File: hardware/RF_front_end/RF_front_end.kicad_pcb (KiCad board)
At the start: 2 copper layers, 42 parts, among them J1 Conn_Coaxial, J2 Conn_Coaxial, Q1 SI1539CDL-T1-GE3, U1 F2972NEGK, U2 TRF37D73, U3 F2972NEGK, U4 RFSA3413, U5 TRF37D73

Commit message: More work on front end
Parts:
- removed C6: 100n, Capacitor_SMD:C_0402_1005Metric
- removed R4: 10k, Resistor_SMD:R_0402_1005Metric
- removed R5: 0, Resistor_SMD:R_0402_1005Metric
- added C21: 10u, Capacitor_SMD:C_0402_1005Metric, F.Cu at (103.8, 107.5)
- added C22: 100n, Capacitor_SMD:C_0402_1005Metric, F.Cu at (105.0, 107.5)
- added C23: 100n, Capacitor_SMD:C_0402_1005Metric, F.Cu at (108.5, 109.8)
- added C24: C, Capacitor_SMD:C_0402_1005Metric, F.Cu at (91.2, 121.5)
- added C25: C, Capacitor_SMD:C_0402_1005Metric, F.Cu at (91.2, 122.8)
- added C26: C, Capacitor_SMD:C_0402_1005Metric, F.Cu at (93.2, 125.0)
- added C27: C, Capacitor_SMD:C_0402_1005Metric, F.Cu at (91.2, 127.2)
- added C28: C, Capacitor_SMD:C_0402_1005Metric, F.Cu at (91.2, 128.5)
- added C29: C, Capacitor_SMD:C_0402_1005Metric, F.Cu at (94.0, 130.0)
- added C30: C, Capacitor_SMD:C_0402_1005Metric, F.Cu at (96.2, 128.0)
- added C31: C, Capacitor_SMD:C_0402_1005Metric, F.Cu at (97.5, 128.0)
- added C32: C, Capacitor_SMD:C_0402_1005Metric, F.Cu at (100.5, 127.5)
- added C33: C, Capacitor_SMD:C_0402_1005Metric, F.Cu at (99.5, 125.2)
- added C34: C, Capacitor_SMD:C_0402_1005Metric, F.Cu at (99.5, 124.0)
- added FB6: FerriteBead_Small, Inductor_SMD:L_0402_1005Metric, F.Cu at (101.2, 107.5)
- added L5: L, Inductor_SMD:L_0603_1608Metric, F.Cu at (91.8, 125.0)
- added L6: L, Inductor_SMD:L_0603_1608Metric, F.Cu at (94.0, 128.5)
- added L7: L, Inductor_SMD:L_0603_1608Metric, F.Cu at (99.0, 127.5)
- added U6: TRF37D73, Package_SON:WSON-8-1EP_2x2mm_P0.5mm_EP0.9x1.6mm, F.Cu at (103.8, 110.0)
- C13: value C -> 100n; footprint Capacitor_SMD:C_0603_1608Metric -> Capacitor_SMD:C_0402_1005Metric
- C14: value C -> 10u; footprint Capacitor_SMD:C_0603_1608Metric -> Capacitor_SMD:C_0402_1005Metric
- C18, C8: value 10u -> 100n; footprint Capacitor_SMD:C_0603_1608Metric -> Capacitor_SMD:C_0402_1005Metric
- C2, C3: footprint Capacitor_SMD:C_0603_1608Metric -> Capacitor_SMD:C_0402_1005Metric
- C9: value 100n -> 10u
- FB2, FB5: footprint Inductor_SMD:L_0603_1608Metric -> Inductor_SMD:L_0402_1005Metric
- L3: value L -> 0603LS-392X_R_
- R2: value 0 -> 10k
- U1, U3: value F2972NEGK -> TRF37D73; footprint RF_WUT:Renesas_QFN-12-1EP_2x2mm_P0.5mm_EP1.1x1.1mm -> Package_SON:WSON-8-1EP_2x2mm_P0.5mm_EP0.9x1.6mm
- U2: value TRF37D73 -> F2972NEGK; footprint Package_SON:WSON-8-1EP_2x2mm_P0.5mm_EP0.9x1.6mm -> RF_WUT:Renesas_QFN-12-1EP_2x2mm_P0.5mm_EP1.1x1.1mm
- U4: value RFSA3413 -> F2972NEGK; footprint Package_DFN_QFN:QFN-16-1EP_3x3mm_P0.5mm_EP1.7x1.7mm_ThermalVias -> RF_WUT:Renesas_QFN-12-1EP_2x2mm_P0.5mm_EP1.1x1.1mm
- U5: value TRF37D73 -> RFSA3413; footprint Package_SON:WSON-8-1EP_2x2mm_P0.5mm_EP0.9x1.6mm -> Package_DFN_QFN:QFN-16-1EP_3x3mm_P0.5mm_EP1.7x1.7mm_ThermalVias
- moved C9 96.9 mm to (89.0, 115.8), turned to 90 degrees
- moved FB5 95.0 mm to (95.2, 119.5)
- moved C4 94.8 mm to (101.8, 121.8)
- moved C11 92.6 mm to (91.8, 119.8), turned to -90 degrees
- moved C8 92.2 mm to (87.8, 115.8), turned to 90 degrees
- moved R1 83.3 mm to (105.8, 117.2), turned to 90 degrees
- moved U5 71.8 mm to (96.5, 115.5), turned to 90 degrees
- moved FB1 71.0 mm to (86.5, 115.8), turned to -90 degrees
- moved R3 66.4 mm to (96.8, 109.2), turned to 90 degrees
- moved C12 65.3 mm to (99.0, 119.8)
- moved C20 65.1 mm to (102.5, 107.5), turned to 90 degrees
- moved C14 64.7 mm to (101.2, 117.2), turned to 180 degrees
- moved C16 64.1 mm to (103.0, 112.8), turned to 180 degrees
- moved C18 63.9 mm to (95.2, 118.2), turned to 180 degrees
- moved C15 63.4 mm to (101.2, 116.0), turned to 180 degrees
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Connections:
- net Net-(C3-Pad1) renamed /20dB Gain Block/RFIN
- C10 pad 2: Net-(C10-Pad2) -> GND
- C11 pad 2: GND -> /20dB Gain Block/RFOUT
- C12 pad 2: Net-(C12-Pad2) -> GND
- C13 pad 1: Net-(C12-Pad2) -> Net-(C13-Pad1)
- C14 pad 1: Net-(C14-Pad1) -> Net-(C13-Pad1)
- C15 pad 1: Net-(C15-Pad1) -> Net-(C13-Pad1)
- C16 pad 2: Net-(C16-Pad2) -> /20dB Gain Block1/RFOUT
- C18 pad 1: Net-(C17-Pad1) -> Net-(C18-Pad1)
- C19 pad 1: Net-(C17-Pad1) -> Net-(C19-Pad1)
- C19 pad 2: GND -> /Adjustable Attenuator/RFOUT
- C20 pad 2: Net-(C20-Pad2) -> GND
- C4 pad 1: Net-(C4-Pad1) -> /RF Switch/RF1
- C4 pad 2: GND -> /20dB Gain Block1/RFIN
- C5 pad 1: Net-(C5-Pad1) -> /RF Switch/RF2
- C5 pad 2: Net-(C5-Pad2) -> /Adjustable Attenuator/RFIN
- C7 pad 1: Net-(C7-Pad1) -> /RF Switch1/RFC
- C7 pad 2: Net-(C7-Pad2) -> /20dB Gain Block2/RFIN
- C8 pad 1: Net-(C6-Pad1) -> Net-(C10-Pad1)
- C9 pad 1: Net-(C6-Pad1) -> Net-(C10-Pad1)
- FB1 pad 2: Net-(C4-Pad1) -> Net-(C10-Pad1)
- FB2 pad 2: Net-(C6-Pad1) -> Net-(C12-Pad1)
- FB3 pad 2: Net-(C11-Pad1) -> Net-(C13-Pad1)
- FB4 pad 2: Net-(C15-Pad1) -> Net-(C17-Pad1)
- FB5 pad 2: Net-(C17-Pad1) -> Net-(C18-Pad1)
- J2 pad 1: Net-(C20-Pad2) -> /20dB Gain Block2/RFOUT
- L2 pad 1: Net-(L2-Pad1) -> Net-(C10-Pad1)
- L2 pad 2: Net-(C10-Pad1) -> Net-(C11-Pad1)
- L3 pad 1: Net-(C12-Pad2) -> Net-(C13-Pad1)
- L3 pad 2: Net-(C14-Pad1) -> Net-(C16-Pad1)
- L4 pad 1: Net-(L4-Pad1) -> Net-(C20-Pad1)
- L4 pad 2: Net-(C20-Pad1) -> Net-(C23-Pad1)
- Q1 pad 2: Net-(Q1-Pad2) -> /ATT_EN
- Q1 pad 6: Net-(Q1-Pad6) -> /RF Switch1/VCTL
- R1 pad 1: Net-(Q1-Pad2) -> /ATT_EN
- R1 pad 2: Net-(R1-Pad2) -> /20dB Gain Block1/PWRDN
- R2 pad 1: Net-(C6-Pad1) -> /ATT_EN
- R2 pad 2: Net-(L2-Pad1) -> GND
- R3 pad 1: Net-(Q1-Pad2) -> +3V3
- R3 pad 2: GND -> /RF Switch1/VCTL
- U1 pad 1: GND -> Net-(C10-Pad1)
- U1 pad 5: Net-(C5-Pad1) -> /20dB Gain Block/PWRDN
- U1 pad 7: Net-(Q1-Pad2) -> Net-(C11-Pad1)
- U1 pad 8: Net-(C4-Pad1) -> GND
- U1 pad 9: Net-(C4-Pad1) -> GND
- U2 pad 1: Net-(C6-Pad1) -> GND
- U2 pad 2: Net-(C5-Pad2) -> /Generic Filter/RFOUT
- U2 pad 5: Net-(R1-Pad2) -> /RF Switch/RF1
- U2 pad 7: Net-(C10-Pad1) -> /ATT_EN
- U2 pad 8: GND -> Net-(C12-Pad1)
- U2 pad 9: GND -> Net-(C12-Pad1)
- U3 pad 1: GND -> Net-(C13-Pad1)
- U3 pad 2: Net-(C12-Pad1) -> /20dB Gain Block1/RFIN
- U3 pad 5: Net-(C7-Pad2) -> /20dB Gain Block1/PWRDN
- U3 pad 7: Net-(Q1-Pad6) -> Net-(C16-Pad1)
- U3 pad 8: Net-(C11-Pad1) -> GND
- U3 pad 9: Net-(C11-Pad1) -> GND
- U4 pad 1: Net-(C15-Pad1) -> GND
- U4 pad 11: Net-(C16-Pad1) -> /20dB Gain Block1/RFOUT
- U4 pad 13: unconnected-(U4-Pad13) -> GND
- U4 pad 2: Net-(C14-Pad1) -> /RF Switch1/RFC
- U4 pad 5: GND -> /Adjustable Attenuator/RFOUT
- U4 pad 7: GND -> /RF Switch1/VCTL
- U4 pad 8: GND -> Net-(C17-Pad1)
- U4 pad 9: GND -> Net-(C17-Pad1)
- U5 pad 1: Net-(C17-Pad1) -> Net-(C18-Pad1)
- U5 pad 2: Net-(C16-Pad2) -> /Adjustable Attenuator/RFIN
- U5 pad 5: unconnected-(U5-Pad5) -> GND
- U5 pad 7: Net-(C20-Pad1) -> GND
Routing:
- net GND: track 9.83 -> 0.00 mm, vias 11 -> 0
- net Net-(C7-Pad2): track 7.76 -> 0.00 mm
- net /20dB Gain Block2/RFOUT: track 0.00 -> 5.77 mm
- net Net-(C10-Pad1): track 3.85 -> 0.00 mm
- net Net-(C1-Pad2): track 3.50 -> 0.00 mm
- net Net-(C23-Pad1): track 0.00 -> 3.35 mm
- net /20dB Gain Block/RFIN: track 3.27 -> 0.00 mm
- net Net-(C5-Pad2): track 1.66 -> 0.00 mm
- net Net-(C10-Pad2): track 1.56 -> 0.00 mm
- net Net-(C7-Pad1): track 1.55 -> 0.00 mm
- net Net-(C5-Pad1): track 1.34 -> 0.00 mm
- net Net-(R1-Pad2): track 1.02 -> 0.00 mm
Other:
- copper layers 2 -> 4

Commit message: Finished front end
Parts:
- added C3: 10u, Capacitor_SMD:C_0603_1608Metric, F.Cu at (78.5, 108.2)
- added C5: 1u, Capacitor_SMD:C_0402_1005Metric, F.Cu at (80.0, 108.5)
- added D1: LED, LED_SMD:LED_0603_1608Metric, F.Cu at (81.8, 110.8)
- added D2: LED, LED_SMD:LED_0603_1608Metric, F.Cu at (84.2, 110.8)
- added D3: LED, LED_SMD:LED_0603_1608Metric, F.Cu at (86.8, 110.8)
- added D4: LED, LED_SMD:LED_0603_1608Metric, F.Cu at (89.2, 110.8)
- added D5: LED, LED_SMD:LED_0603_1608Metric, F.Cu at (91.8, 110.8)
- added FB1: FerriteBead_Small, Inductor_SMD:L_0603_1608Metric, F.Cu at (76.5, 108.2)
- added J2: Conn_01x07_Male, Connector_PinHeader_2.54mm:PinHeader_1x07_P2.54mm_Vertical, F.Cu at (76.5, 104.8)
- added M1: Logo_10mmx10mm, Misc_WUT:Logo_10mmx10mm, F.Cu at (109.0, 125.2)
- added R1: 1k, Resistor_SMD:R_0402_1005Metric, F.Cu at (81.8, 108.0)
- added R10: 100, Resistor_SMD:R_0402_1005Metric, F.Cu at (90.5, 108.0)
- added R2: 1k, Resistor_SMD:R_0402_1005Metric, F.Cu at (84.2, 108.0)
- added R3: 1k, Resistor_SMD:R_0402_1005Metric, F.Cu at (86.8, 108.0)
- added R4: 1k, Resistor_SMD:R_0402_1005Metric, F.Cu at (89.2, 108.0)
- added R5: 1k, Resistor_SMD:R_0402_1005Metric, F.Cu at (91.8, 108.0)
- added R6: 100, Resistor_SMD:R_0402_1005Metric, F.Cu at (83.0, 108.0)
- added R7: 100, Resistor_SMD:R_0402_1005Metric, F.Cu at (88.0, 108.0)
- added R8: 100, Resistor_SMD:R_0402_1005Metric, F.Cu at (93.0, 108.0)
- added R9: 100, Resistor_SMD:R_0402_1005Metric, F.Cu at (85.5, 108.0)
- U5: footprint Package_DFN_QFN:QFN-16-1EP_3x3mm_P0.5mm_EP1.7x1.7mm_ThermalVias -> Package_DFN_QFN:QFN-16-1EP_3x3mm_P0.5mm_EP1.7x1.7mm
- moved R12 5.64 mm to (97.2, 110.5), turned to 180 degrees
- moved R13 3.29 mm to (97.2, 106.0), turned to 180 degrees
- moved Q1 3.16 mm to (97.2, 108.2), turned to 90 degrees
- moved C17 0.56 mm to (103.5, 113.0), turned to 90 degrees
- moved C19 0.50 mm to (94.8, 118.2)
- moved C24 0.50 mm to (108.0, 109.8)
- moved FB6 0.50 mm to (94.8, 119.5)
- moved C12 0.25 mm to (91.8, 119.5)
- moved C13 0.25 mm to (98.8, 119.8)
- moved FB3 0.25 mm to (98.8, 118.5)
- moved L2 0.25 mm to (91.5, 117.0)
- moved L3 0.25 mm to (102.8, 114.8)
- moved L4 0.25 mm to (106.2, 109.0)
- renumbered C9 to C10, C10 to C11, C11 to C12, C12 to C13, C13 to C14, C14 to C15, C15 to C16, C16 to C17, C17 to C18, C18 to C19, C19 to C20, C20 to C21, C21 to C22, C22 to C23, C23 to C24, C24 to C25, C25 to C26, C26 to C27, C27 to C28, C28 to C29, C29 to C30, C30 to C31, C31 to C32, C32 to C33, C33 to C34, C34 to C35, C3 to C4, C4 to C6, C5 to C7, C7 to C8, C8 to C9, FB1 to FB2, FB2 to FB3, FB3 to FB4, FB4 to FB5, FB5 to FB6, FB6 to FB7, J2 to J3, R1 to R11, R2 to R12, R3 to R13
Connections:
- U5 pad 13: /Adjustable Attenuator/ATT3 -> /ATT3
- U5 pad 14: /Adjustable Attenuator/ATT2 -> /ATT2
- U5 pad 15: /Adjustable Attenuator/ATT1 -> /ATT1
- U5 pad 16: /Adjustable Attenuator/ATT0 -> /ATT0
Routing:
- net GND: track 0.00 -> 54.0 mm, vias 0 -> 82
- net /ATT_EN: track 0.00 -> 29.3 mm, vias 0 -> 3
- net /ATT0: track 0.00 -> 18.1 mm, vias 0 -> 2
- net /ATT1: track 0.00 -> 15.4 mm, vias 0 -> 2
- net +3V3: track 0.00 -> 12.4 mm, vias 0 -> 14
- net /ATT2: track 0.00 -> 12.3 mm, vias 0 -> 2
- net /RF Switch1/VCTL: track 0.00 -> 9.77 mm, vias 0 -> 2
- net /ATT3: track 0.00 -> 9.46 mm, vias 0 -> 2
- net Net-(C30-Pad2): track 0.00 -> 7.56 mm
- net Net-(C27-Pad2): track 0.00 -> 7.46 mm
- net Net-(C21-Pad1): track 0.00 -> 6.74 mm
- net Net-(C14-Pad1): track 0.00 -> 6.74 mm
- net Net-(C10-Pad1): track 0.00 -> 6.65 mm
- net /Generic Filter/RFOUT: track 0.00 -> 5.64 mm
- net /20dB Gain Block/RFOUT: track 0.00 -> 5.63 mm
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- added copper zone on In2.Cu, net +3V3
- added copper zone on B.Cu, net GND
- added copper zone on In1.Cu, net GND
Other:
- board outline added: 42.2 x 31.2 mm
- board text added: "0V"
- board text added: "1"
- board text added: "2"
- board text added: "3V3"
- board text added: "4"
- board text added: "8"
- board text added: "EN"
- board text added: "SDR Front End v0.1 10/6/21 M0WUT"

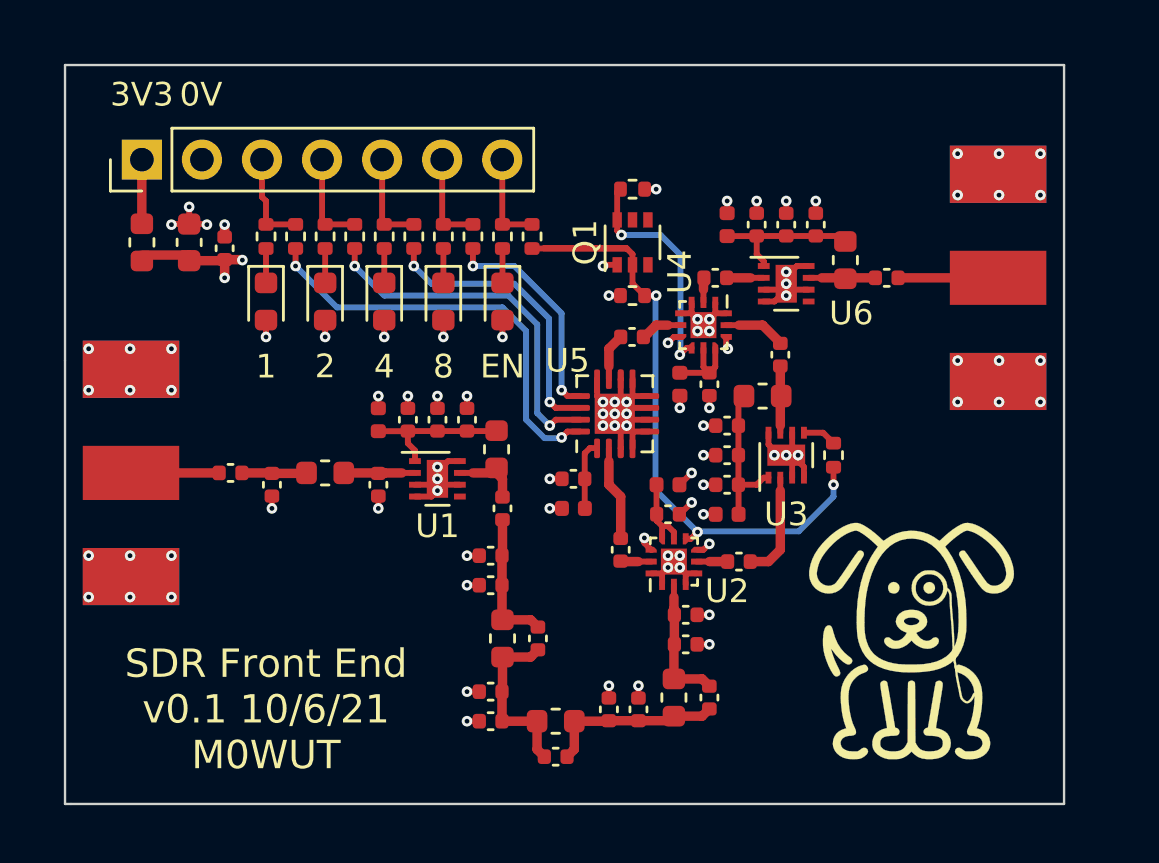
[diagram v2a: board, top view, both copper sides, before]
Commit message: Faffed with moving more stuff into config files. Now locks up when reading temperature
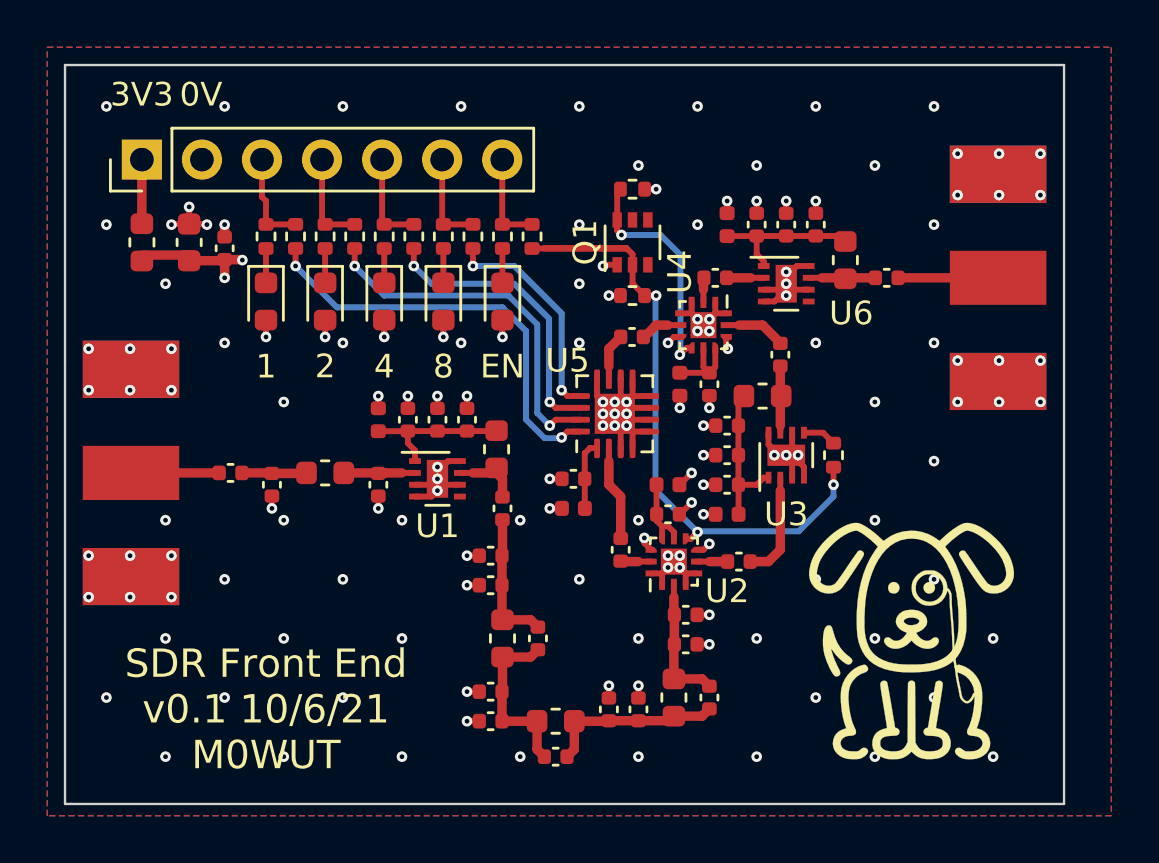
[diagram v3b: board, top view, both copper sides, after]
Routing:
- net GND: vias 82 -> 139
- added copper zone on F.Cu, net GND
